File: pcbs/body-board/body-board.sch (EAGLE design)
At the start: 29 parts, among them X1 2520-

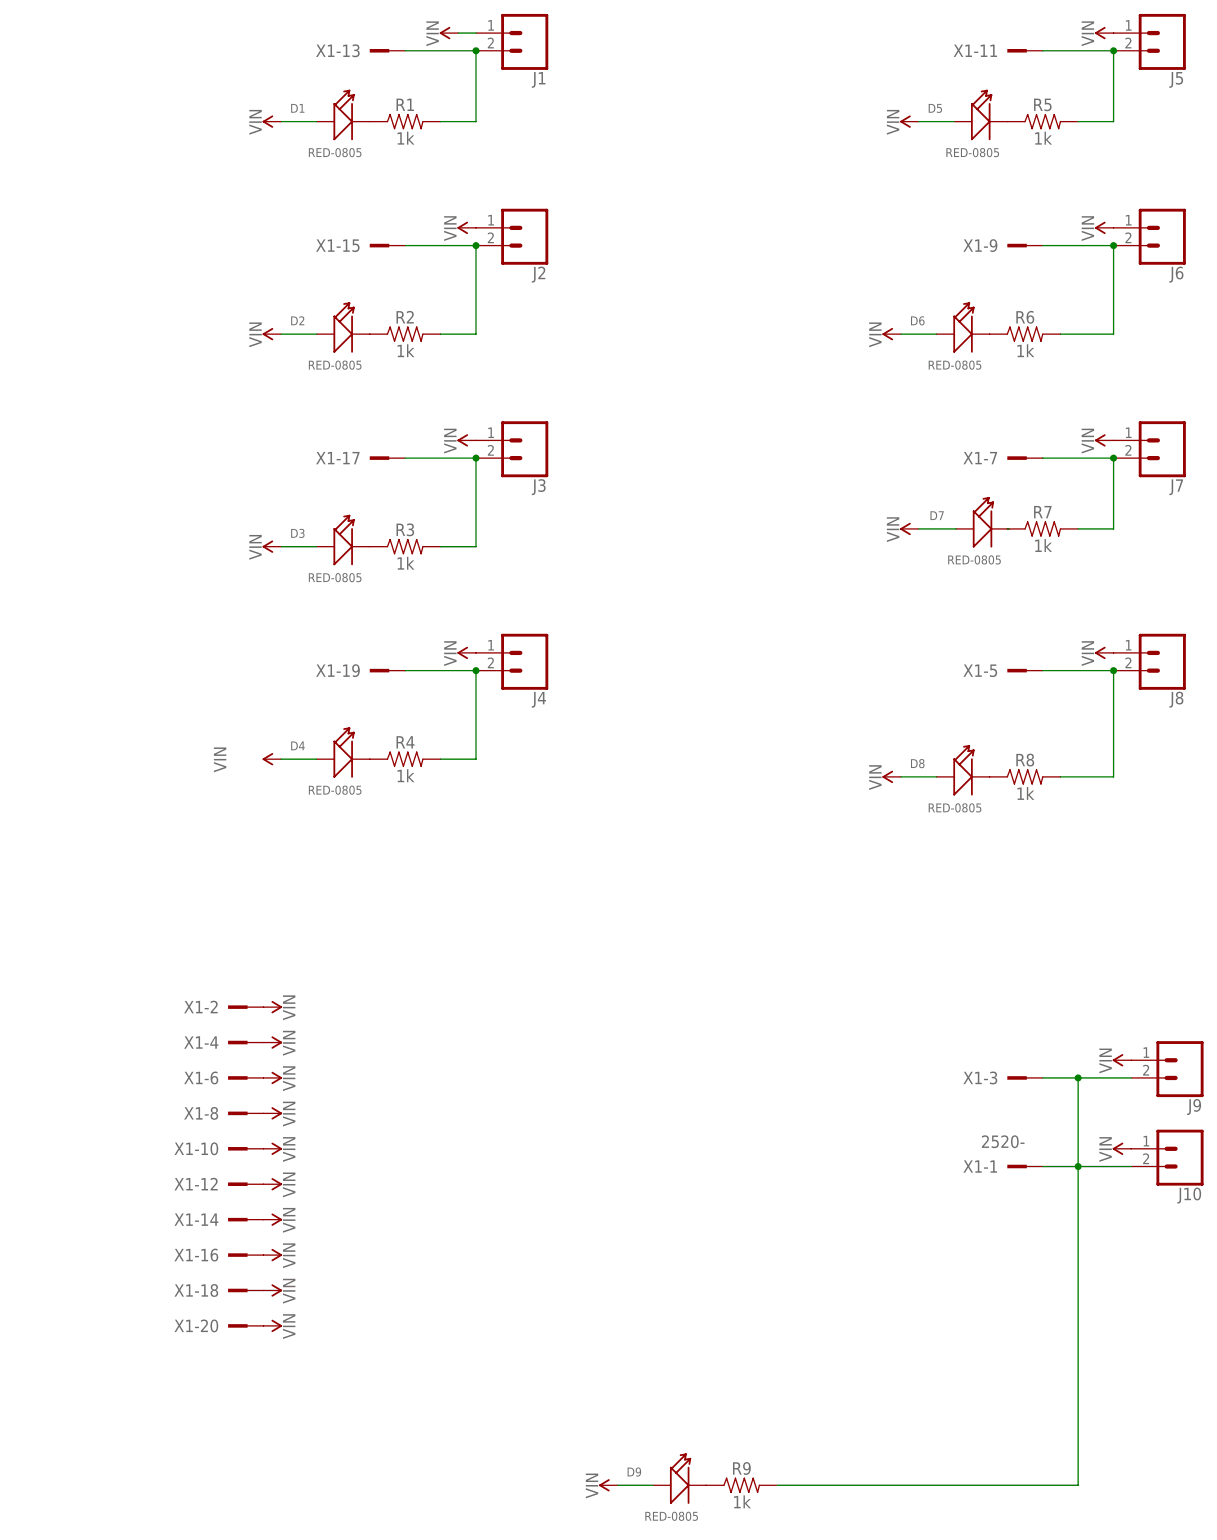
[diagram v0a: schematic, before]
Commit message: Update bom and exported schematics
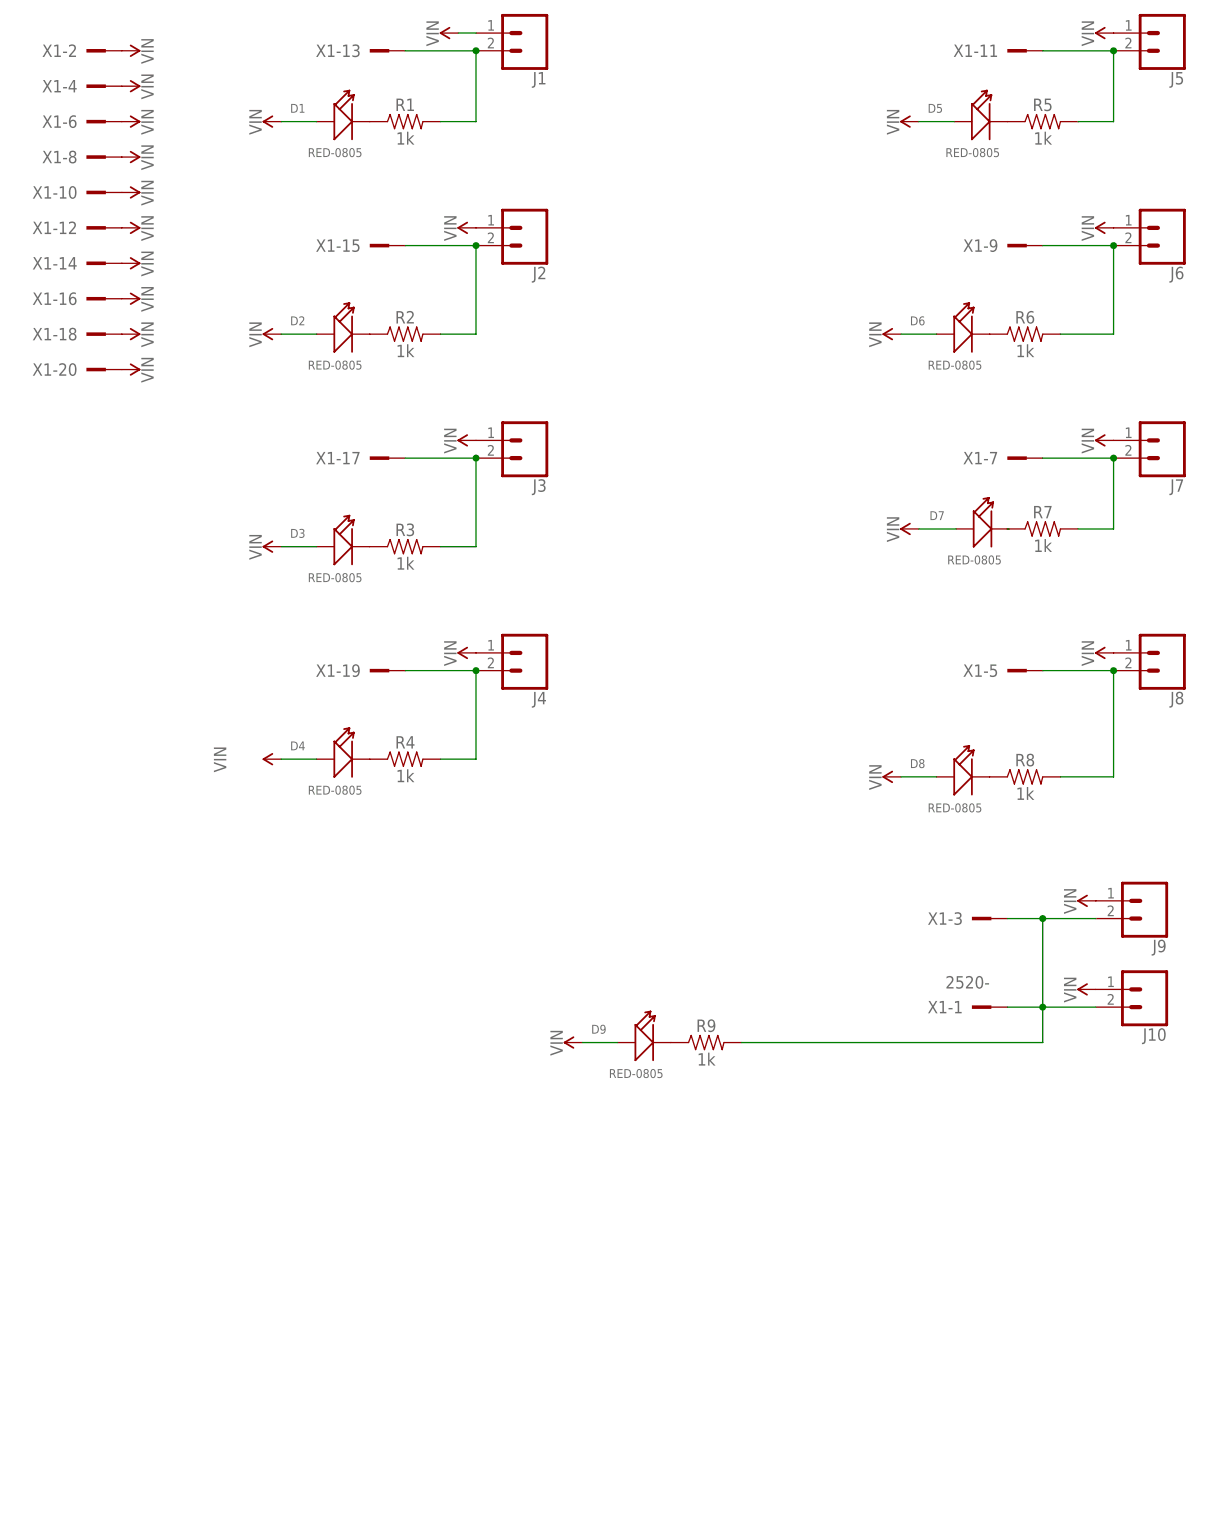
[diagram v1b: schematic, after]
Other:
- moved on the sheet: D9, J10, J9, R9, X1-1, X1-10, X1-12, X1-14, X1-16, X1-18, X1-2, X1-20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

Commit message: Update boards to latest
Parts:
- J1, J10, J2, J3, J4, J5, J6, J7, J8, J9: device SparkFun-Connectors:CONN_02JST-PTH-2 -> SparkFun-Connectors:CONN_022.54MM_SCREWTERM
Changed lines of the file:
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@@
 <parts>
 <part name="X1" library="con-3m" library_urn="urn:adsk.eagle:library:119" deviceset="2520-" device="" package3d_urn="urn:adsk.eagle:package:5578/1"/>
-<part name="J1" library="SparkFun-Connectors" library_urn="urn:adsk.eagle:library:513" deviceset="CONN_02" device="JST-PTH-2" package3d_urn="urn:adsk.eagle:package:38053/1"/>
-<part name="J2" library="SparkFun-Connectors" library_urn="urn:adsk.eagle:library:513" deviceset="CONN_02" device="JST-PTH-2" package3d_urn="urn:adsk.eagle:package:38053/1"/>
-<part name="J3" library="SparkFun-Connectors" library_urn="urn:adsk.eagle:library:513" deviceset="CONN_02" device="JST-PTH-2" package3d_urn="urn:adsk.eagle:package:38053/1"/>
-<part name="J4" library="SparkFun-Connectors" library_urn="urn:adsk.eagle:library:513" deviceset="CONN_02" device="JST-PTH-2" package3d_urn="urn:adsk.eagle:package:38053/1"/>
-<part name="J5" library="SparkFun-Connectors" library_urn="urn:adsk.eagle:library:513" deviceset="CONN_02" device="JST-PTH-2" package3d_urn="urn:adsk.eagle:package:38053/1"/>
-<part name="J6" library="SparkFun-Connectors" library_urn="urn:adsk.eagle:library:513" deviceset="CONN_02" device="JST-PTH-2" package3d_urn="urn:adsk.eagle:package:38053/1"/>
-<part name="J7" library="SparkFun-Connectors" library_urn="urn:adsk.eagle:library:513" deviceset="CONN_02" device="JST-PTH-2" package3d_urn="urn:adsk.eagle:package:38053/1"/>
-<part name="J8" library="SparkFun-Connectors" library_urn="urn:adsk.eagle:library:513" deviceset="CONN_02" device="JST-PTH-2" package3d_urn="urn:adsk.eagle:package:38053/1"/>
-<part name="J9" library="SparkFun-Connectors" library_urn="urn:adsk.eagle:library:513" deviceset="CONN_02" device="JST-PTH-2" package3d_urn="urn:adsk.eagle:package:38053/1"/>
-<part name="J10" library="SparkFun-Connectors" library_urn="urn:adsk.eagle:library:513" deviceset="CONN_02" device="JST-PTH-2" package3d_urn="urn:adsk.eagle:package:38053/1"/>
+<part name="J1" library="SparkFun-Connectors" library_urn="urn:adsk.eagle:library:513" deviceset="CONN_02" device="2.54MM_SCREWTERM" package3d_urn="urn:adsk.eagle:package:38059/1"/>
+<part name="J2" library="SparkFun-Connectors" library_urn="urn:adsk.eagle:library:513" deviceset="CONN_02" device="2.54MM_SCREWTERM" package3d_urn="urn:adsk.eagle:package:38059/1"/>
+<part name="J3" library="SparkFun-Connectors" library_urn="urn:adsk.eagle:library:513" deviceset="CONN_02" device="2.54MM_SCREWTERM" package3d_urn="urn:adsk.eagle:package:38059/1"/>
+<part name="J4" library="SparkFun-Connectors" library_urn="urn:adsk.eagle:library:513" deviceset="CONN_02" device="2.54MM_SCREWTERM" package3d_urn="urn:adsk.eagle:package:38059/1"/>
+<part name="J5" library="SparkFun-Connectors" library_urn="urn:adsk.eagle:library:513" deviceset="CONN_02" device="2.54MM_SCREWTERM" package3d_urn="urn:adsk.eagle:package:38059/1"/>
+<part name="J6" library="SparkFun-Connectors" library_urn="urn:adsk.eagle:library:513" deviceset="CONN_02" device="2.54MM_SCREWTERM" package3d_urn="urn:adsk.eagle:package:38059/1"/>
+<part name="J7" library="SparkFun-Connectors" library_urn="urn:adsk.eagle:library:513" deviceset="CONN_02" device="2.54MM_SCREWTERM" package3d_urn="urn:adsk.eagle:package:38059/1"/>
+<part name="J8" library="SparkFun-Connectors" library_urn="urn:adsk.eagle:library:513" deviceset="CONN_02" device="2.54MM_SCREWTERM" package3d_urn="urn:adsk.eagle:package:38059/1"/>
+<part name="J9" library="SparkFun-Connectors" library_urn="urn:adsk.eagle:library:513" deviceset="CONN_02" device="2.54MM_SCREWTERM" package3d_urn="urn:adsk.eagle:package:38059/1"/>
+<part name="J10" library="SparkFun-Connectors" library_urn="urn:adsk.eagle:library:513" deviceset="CONN_02" device="2.54MM_SCREWTERM" package3d_urn="urn:adsk.eagle:package:38059/1"/>
 <part name="D1" library="OPL_Optoelectronics" library_urn="urn:adsk.eagle:library:8004780" deviceset="SMD-LED-CLEAR-RED(0805)" device="" package3d_urn="urn:adsk.eagle:package:8004829/1" value="RED-0805"/>
 <part name="D2" library="OPL_Optoelectronics" library_urn="urn:adsk.eagle:library:8004780" deviceset="SMD-LED-CLEAR-RED(0805)" device="" package3d_urn="urn:adsk.eagle:package:8004829/1" value="RED-0805"/>

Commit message: Updated body board sans creation crate logo
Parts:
- removed D9: RED-0805, OPL_Optoelectronics:SMD-LED-CLEAR-RED(0805)
- removed R9: 1k, SparkFun-Resistors:1KOHM-0603-1/10W-1%
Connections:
- removed net N$7: D9.-, R9.1
- net N$8: no longer R9.2
- net VIN: no longer D9.+
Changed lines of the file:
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@@
 <part name="D7" library="OPL_Optoelectronics" library_urn="urn:adsk.eagle:library:8004780" deviceset="SMD-LED-CLEAR-RED(0805)" device="" package3d_urn="urn:adsk.eagle:package:8004829/1" value="RED-0805"/>
 <part name="D8" library="OPL_Optoelectronics" library_urn="urn:adsk.eagle:library:8004780" deviceset="SMD-LED-CLEAR-RED(0805)" device="" package3d_urn="urn:adsk.eagle:package:8004829/1" value="RED-0805"/>
-<part name="D9" library="OPL_Optoelectronics" library_urn="urn:adsk.eagle:library:8004780" deviceset="SMD-LED-CLEAR-RED(0805)" device="" package3d_urn="urn:adsk.eagle:package:8004829/1" value="RED-0805"/>
 <part name="R1" library="SparkFun-Resistors" library_urn="urn:adsk.eagle:library:532" deviceset="1KOHM" device="-0603-1/10W-1%" package3d_urn="urn:adsk.eagle:package:39650/1" value="1k"/>
 <part name="R2" library="SparkFun-Resistors" library_urn="urn:adsk.eagle:library:532" deviceset="1KOHM" device="-0603-1/10W-1%" package3d_urn="urn:adsk.eagle:package:39650/1" value="1k"/>
@@
 <part name="R7" library="SparkFun-Resistors" library_urn="urn:adsk.eagle:library:532" deviceset="1KOHM" device="-0603-1/10W-1%" package3d_urn="urn:adsk.eagle:package:39650/1" value="1k"/>
 <part name="R8" library="SparkFun-Resistors" library_urn="urn:adsk.eagle:library:532" deviceset="1KOHM" device="-0603-1/10W-1%" package3d_urn="urn:adsk.eagle:package:39650/1" value="1k"/>
-<part name="R9" library="SparkFun-Resistors" library_urn="urn:adsk.eagle:library:532" deviceset="1KOHM" device="-0603-1/10W-1%" package3d_urn="urn:adsk.eagle:package:39650/1" value="1k"/>
 <part name="SUPPLY1" library="SparkFun-PowerSymbols" library_urn="urn:adsk.eagle:library:530" deviceset="VIN" device=""/>
 <part name="SUPPLY2" library="SparkFun-PowerSymbols" library_urn="urn:adsk.eagle:library:530" deviceset="VIN" device=""/>
@@
 <part name="SUPPLY27" library="SparkFun-PowerSymbols" library_urn="urn:adsk.eagle:library:530" deviceset="VIN" device=""/>
 <part name="SUPPLY28" library="SparkFun-PowerSymbols" library_urn="urn:adsk.eagle:library:530" deviceset="VIN" device=""/>
-<part name="SUPPLY29" library="SparkFun-PowerSymbols" library_urn="urn:adsk.eagle:library:530" deviceset="VIN" device=""/>
 </parts>
 <sheets>
@@
 <attribute name="VALUE" x="46.99" y="40.64" size="1.27" layer="96" ratio="10"/>
 </instance>
-<instance part="D9" gate="G$1" x="6.35" y="7.62" smashed="yes">
-<attribute name="NAME" x="-1.27" y="8.89" size="1.27" layer="95" ratio="10"/>
-<attribute name="VALUE" x="1.27" y="2.54" size="1.27" layer="96" ratio="10"/>
-</instance>
 <instance part="R1" gate="G$1" x="-27.94" y="139.7" smashed="yes">
 <attribute name="NAME" x="-27.94" y="141.224" size="1.778" layer="95" font="vector" align="bottom-center"/>
@@
 <attribute name="VALUE" x="60.96" y="44.196" size="1.778" layer="96" font="vector" align="top-center"/>
 </instance>
-<instance part="R9" gate="G$1" x="15.24" y="7.62" smashed="yes">
-<attribute name="NAME" x="15.24" y="9.144" size="1.778" layer="95" font="vector" align="bottom-center"/>
-<attribute name="VALUE" x="15.24" y="6.096" size="1.778" layer="96" font="vector" align="top-center"/>
-</instance>
 <instance part="SUPPLY1" gate="G$1" x="-68.58" y="149.86" smashed="yes" rot="R270">
 <attribute name="VALUE" x="-65.786" y="149.86" size="1.778" layer="96" rot="R270" align="bottom-center"/>
@@
 <instance part="SUPPLY28" gate="G$1" x="43.18" y="45.72" smashed="yes" rot="R90">
 <attribute name="VALUE" x="40.386" y="45.72" size="1.778" layer="96" rot="R90" align="bottom-center"/>
-</instance>
-<instance part="SUPPLY29" gate="G$1" x="-2.54" y="7.62" smashed="yes" rot="R90">
-<attribute name="VALUE" x="-5.334" y="7.62" size="1.778" layer="96" rot="R90" align="bottom-center"/>
 </instance>
 </instances>
@@
 </segment>
 </net>
-<net name="N$7" class="0">
-<segment>
-<pinref part="R9" gate="G$1" pin="1"/>
-<pinref part="D9" gate="G$1" pin="-"/>
-</segment>
-</net>
 <net name="VIN" class="0">
 <segment>
@@
 <pinref part="SUPPLY26" gate="G$1" pin="VIN"/>
 <wire x1="43.18" y1="109.22" x2="48.26" y2="109.22" width="0.1524" layer="91"/>
-</segment>
-<segment>
-<pinref part="D9" gate="G$1" pin="+"/>
-<pinref part="SUPPLY29" gate="G$1" pin="VIN"/>
-<wire x1="-2.54" y1="7.62" x2="2.54" y2="7.62" width="0.1524" layer="91"/>
 </segment>
 <segment>
@@
 <junction x="63.5" y="12.7"/>
 <junction x="63.5" y="25.4"/>
-<pinref part="R9" gate="G$1" pin="2"/>
-<wire x1="63.5" y1="12.7" x2="63.5" y2="7.62" width="0.1524" layer="91"/>
-<wire x1="63.5" y1="7.62" x2="20.32" y2="7.62" width="0.1524" layer="91"/>
-</segment>
-</net>
+</segment>
+</net>
